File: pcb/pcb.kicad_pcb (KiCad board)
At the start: 2 copper layers, 60 x 30 mm, 30 parts, among them J1 USB_B_Mini, J2 Conn_01x04_Male, SW1 OS102011MA1QN1‎, SW1 PTS645Vx83, SW2 PTS645Vx83, SW3 PTS645Vx83, U1 AP2112K-3.3, U2 MIC5225-1.8YM5, U3 CP2104, U5 ESP-12F

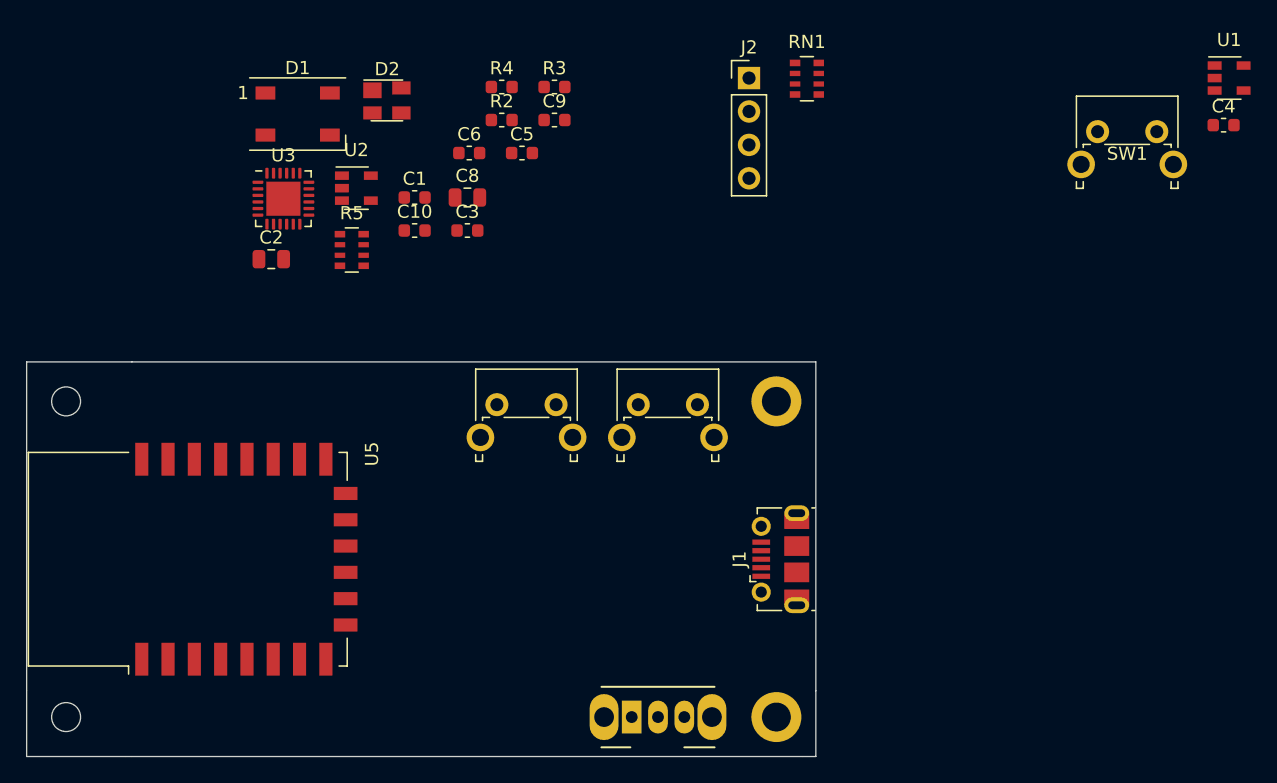
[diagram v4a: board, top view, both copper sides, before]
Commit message: finish laying out most of the pcb parts
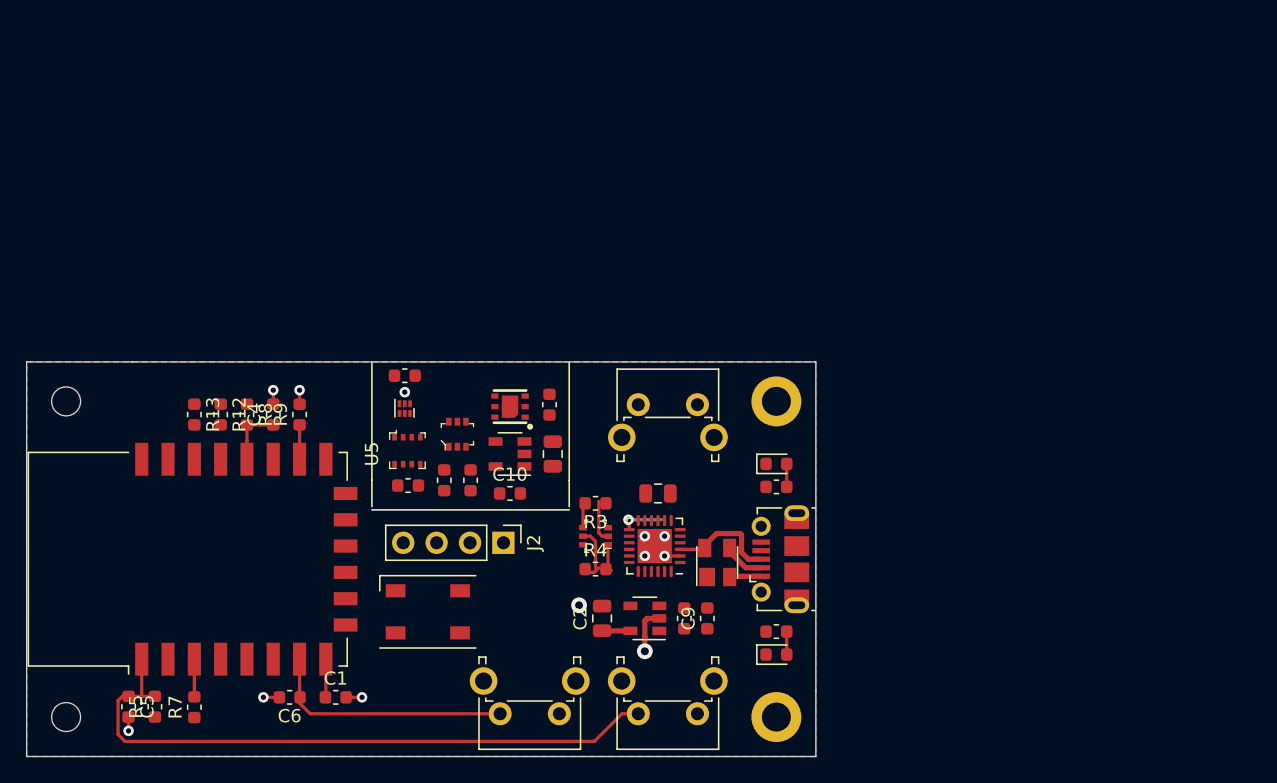
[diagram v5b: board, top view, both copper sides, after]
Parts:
- removed RN1: 10k, Resistor_SMD:R_Array_Convex_4x0603
- removed the SW1 at (86.0, 82.0)
- added C11: 100n, Capacitor_SMD:C_0603_1608Metric, F.Cu at (68.8, 56.0)
- added C12: 100n, Capacitor_SMD:C_0603_1608Metric, F.Cu at (79.8, 58.2)
- added C7: 10u, Capacitor_SMD:C_0805_2012Metric, F.Cu at (88.0, 65.0)
- added D3: LED, LED_SMD:LED_0603_1608Metric, F.Cu at (97.0, 62.8)
- added D4: LED, LED_SMD:LED_0603_1608Metric, F.Cu at (97.0, 77.2)
- added Q1: BSS138DW-7-F, digikey-footprints:SOT-363, F.Cu at (83.2, 68.2)
- added Q2: BSS138DW-7-F, digikey-footprints:SOT-363, F.Cu at (72.8, 60.5)
- added R1: 470, Resistor_SMD:R_0603_1608Metric, F.Cu at (97.0, 64.5)
- added R10: 10k, Resistor_SMD:R_0603_1608Metric, F.Cu at (71.8, 64.0)
- added R11: 10k, Resistor_SMD:R_0603_1608Metric, F.Cu at (73.8, 64.0)
- added R12: 10k, Resistor_SMD:R_0603_1608Metric, F.Cu at (54.8, 59.0)
- added R13: 10k, Resistor_SMD:R_0603_1608Metric, F.Cu at (52.8, 59.0)
- added R6: 470, Resistor_SMD:R_0603_1608Metric, F.Cu at (97.0, 75.5)
- added R7: 10k, Resistor_SMD:R_0603_1608Metric, F.Cu at (52.8, 81.2)
- added R8: 10k, Resistor_SMD:R_0603_1608Metric, F.Cu at (56.8, 59.0)
- added R9: 10k, Resistor_SMD:R_0603_1608Metric, F.Cu at (60.8, 59.0)
- added U4: BME280, digikey-footprints:Pressure_Sensor_LGA-8_2.5x2.5mm_BME280, F.Cu at (69.0, 61.8)
- added U6: SGP30, SGP30 (1):SGP30, F.Cu at (76.8, 58.4)
- added U7: TSL2591, Package_DFN_QFN:DFN-6_1.3x1.2mm_P0.4mm, F.Cu at (68.8, 58.5)
- C10: value 1u -> 10u
- C9: value 100n -> 10u
- R5: footprint Resistor_SMD:R_Array_Convex_4x0603 -> Resistor_SMD:R_0603_1608Metric
- moved C4 75.5 mm to (58.8, 59.0), turned to 90 degrees
- moved U1 60.5 mm to (87.0, 74.5), turned to 180 degrees
- moved SW1 60.3 mm to (80.5, 81.8), turned to 180 degrees
- moved C5 51.6 mm to (47.8, 81.2), turned to 270 degrees
- moved C6 43.6 mm to (60.0, 80.5), turned to 180 degrees
- moved D2 43.2 mm to (92.5, 70.2), turned to 90 degrees
- moved R2 40.4 mm to (90.0, 74.5), turned to 90 degrees
- moved J2 40.0 mm to (76.2, 68.8), turned to 270 degrees
- moved C9 39.6 mm to (91.8, 74.5), turned to 90 degrees
- moved D1 39.1 mm to (70.5, 74.0), turned to 180 degrees
- moved U3 38.7 mm to (87.8, 69.0), turned to 180 degrees
- moved C1 38.5 mm to (63.5, 80.5)
- moved R5 37.8 mm to (49.8, 81.2), turned to 90 degrees
- moved R4 37.3 mm to (83.2, 70.8)
- moved C2 37.1 mm to (83.8, 74.5), turned to 90 degrees
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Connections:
- C1 pad 1: nRST -> +3V3
- C3 pad 1: +5V -> +3V3
- C9 pad 1: +3V3 -> +5V
- D2 pad 2: Net-(D2-Pad2) -> +5V
- D2 pad 4: +5V -> Net-(D2-Pad4)
- J1 pad 3: Net-(D2-Pad2) -> Net-(D2-Pad4)
- R3 pad 1: (no net) -> Net-(Q1-Pad2)
- R4 pad 1: (no net) -> Net-(Q1-Pad5)
- R5 pad 1: Net-(R5-Pad1) -> +3V3
- SW1 pad 2: nBOOT -> MODE
- SW2 pad 2: nRST -> nBOOT
- SW3 pad 2: MODE -> nRST
- U2 pad 1: +3V3 -> +5V
- U2 pad 3: +3V3 -> +5V
- U3 pad 13: (no net) -> Net-(R1-Pad2)
- U3 pad 14: (no net) -> Net-(R6-Pad2)
- U3 pad 3: Net-(D2-Pad2) -> Net-(D2-Pad4)
- U5 pad 13: (no net) -> nINT
- U5 pad 14: MODE -> (no net)
- U5 pad 16: Net-(R5-Pad5) -> Net-(R9-Pad1)
- U5 pad 3: Net-(R5-Pad1) -> Net-(R7-Pad2)
- U5 pad 7: (no net) -> MODE
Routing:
- net nRST: track 0.00 -> 49.0 mm
- net MODE: track 0.00 -> 18.9 mm
- net GND: track 0.00 -> 14.0 mm, vias 0 -> 11
- net Net-(D2-Pad4): track 0.00 -> 8.37 mm
- net +3V3: track 0.00 -> 5.27 mm
- net nBOOT: track 0.00 -> 4.61 mm
- net Net-(Q1-Pad5): track 0.00 -> 4.05 mm
- net Net-(Q1-Pad2): track 0.00 -> 3.78 mm
- net Net-(R1-Pad2): track 0.00 -> 3.27 mm, vias 0 -> 1
- net Net-(D2-Pad3): track 0.00 -> 3.18 mm
- net Net-(R7-Pad2): track 0.00 -> 2.86 mm
- net Net-(R9-Pad1): track 0.00 -> 2.61 mm
- net Net-(Q1-Pad1): track 0.00 -> 2.26 mm
- net +5V: track 0.00 -> 2.17 mm
- net Net-(Q1-Pad4): track 0.00 -> 2.17 mm
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- added copper zone on F.Cu, net +3V3
- added copper zone on B.Cu, net GND

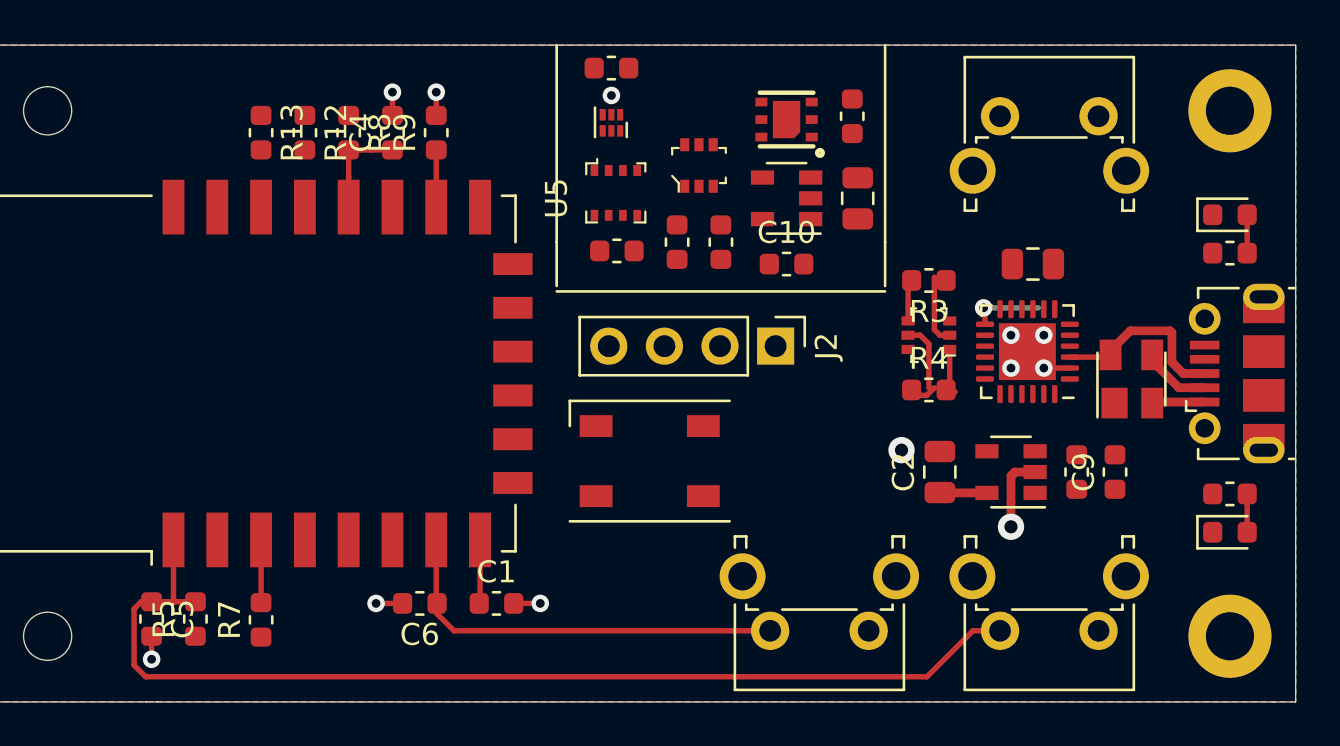
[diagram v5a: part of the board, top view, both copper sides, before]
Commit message: finish the routing of the pcb all that is left is to clean up the silkscreen
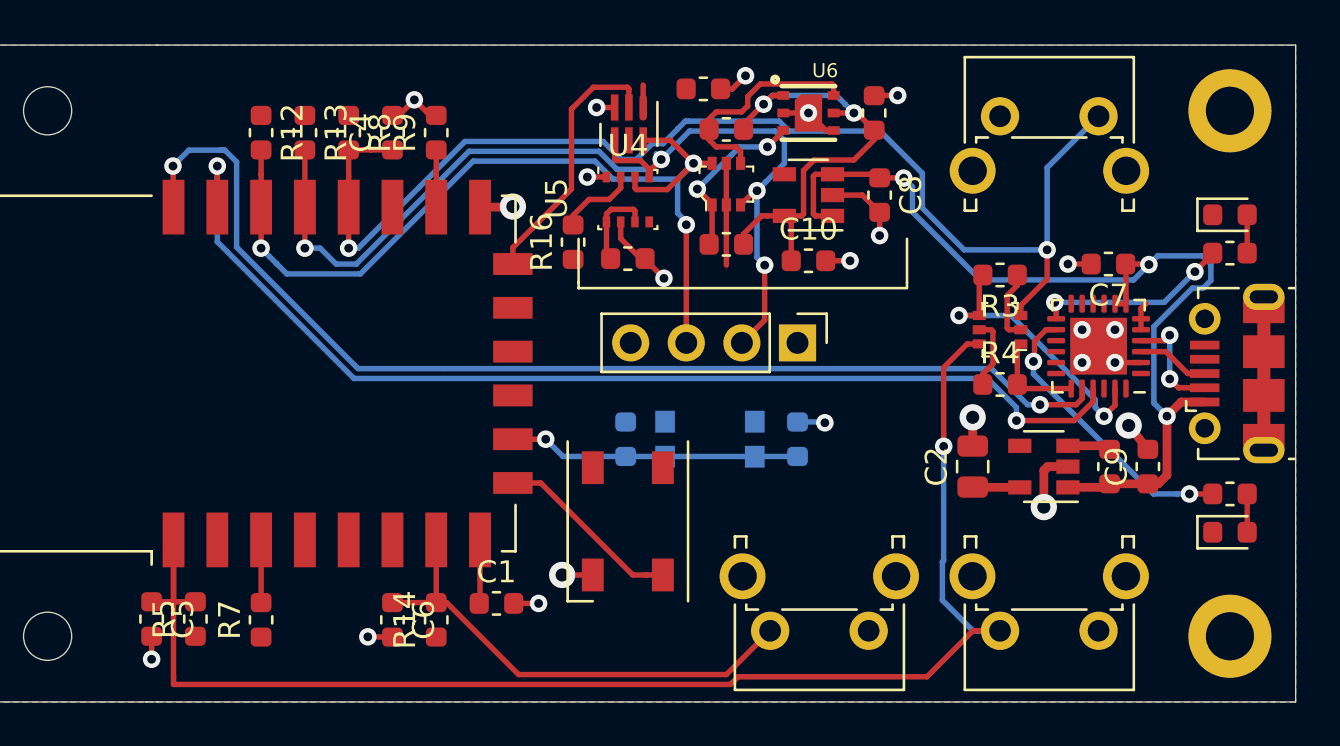
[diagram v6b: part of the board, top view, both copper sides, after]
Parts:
- removed D2: SP0503BAHT, Package_TO_SOT_SMD:SOT-143
- added C13: 100n, Capacitor_SMD:C_0603_1608Metric, B.Cu at (69.4, 73.0)
- added R14: 10k, Resistor_SMD:R_0603_1608Metric, F.Cu at (60.8, 81.2)
- added R15: 10k, Resistor_SMD:R_0603_1608Metric, B.Cu at (77.2, 73.0)
- added R16: 10k, Resistor_SMD:R_0603_1608Metric, F.Cu at (67.0, 64.0)
- added SW4: KMR2, Button_Switch_SMD:SW_Push_1P1T_NO_CK_KMR2, B.Cu at (73.2, 73.0)
- C7, C8: footprint Capacitor_SMD:C_0805_2012Metric -> Capacitor_SMD:C_0603_1608Metric
- U4: footprint digikey-footprints:Pressure_Sensor_LGA-8_2.5x2.5mm_BME280 -> Package_LGA:Bosch_LGA-8_2.5x2.5mm_P0.65mm_ClockwisePinNumbering
- U7: footprint Package_DFN_QFN:DFN-6_1.3x1.2mm_P0.4mm -> Kevin-Lutzer-Kicad-Lbr:TSL2591
- moved R11 5.16 mm to (74.0, 58.9), turned to 180 degrees
- moved C11 4.31 mm to (73.0, 57.0), turned to 0 degrees
- moved C7 3.45 mm to (91.5, 65.0)
- moved Q1 3.26 mm to (86.5, 68.0)
- moved R3 3.26 mm to (86.5, 65.5)
- moved R4 3.26 mm to (86.5, 70.5)
- moved U3 3.26 mm to (91.0, 68.8)
- moved D1 2.93 mm to (69.5, 76.8), turned to 270 degrees
- moved R10 2.25 mm to (74.0, 64.1), turned to 180 degrees
- moved R12 2.00 mm to (52.8, 59.0)
- moved R13 2.00 mm to (54.8, 59.0)
- moved C2 1.52 mm to (85.2, 74.2)
- moved C9 1.52 mm to (93.2, 74.2)
- moved R2 1.52 mm to (91.5, 74.2)
- moved U1 1.52 mm to (88.5, 74.2)
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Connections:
- net MODE renamed nMODE
- U4 pad 2: (no net) -> Net-(R16-Pad2)
- U5 pad 10: (no net) -> nFAC_RST
- U5 pad 13: nINT -> (no net)
- U5 pad 14: (no net) -> nINT
- U5 pad 17: RGB_LED -> (no net)
- U5 pad 9: (no net) -> RGB_LED
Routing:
- net UART_RX: track 0.00 -> 51.7 mm, vias 0 -> 2
- net nBOOT: track 4.61 -> 55.4 mm, vias 0 -> 2
- net UART_TX: track 0.00 -> 50.0 mm, vias 0 -> 2
- net I2C_SCK: track 0.00 -> 45.8 mm, vias 0 -> 4
- net I2C_SDA: track 0.00 -> 43.4 mm, vias 0 -> 3
- net +5V: track 2.17 -> 45.5 mm, vias 0 -> 3
- net GND: track 14.0 -> 39.7 mm, vias 11 -> 22
- net +1V8: track 0.00 -> 21.7 mm, vias 0 -> 2
- net nRST: track 49.0 -> 66.1 mm, vias 0 -> 1
- net nFAC_RST: track 0.00 -> 13.3 mm, vias 0 -> 1
- net Net-(R6-Pad2): track 0.07 -> 13.2 mm, vias 0 -> 2
- net +3V3: track 5.27 -> 17.5 mm, vias 0 -> 1
- net nINT: track 0.00 -> 12.1 mm, vias 1 -> 0
- net Net-(Q1-Pad4): track 2.17 -> 13.1 mm, vias 0 -> 2
- net I2C_SCK_1V8: track 0.00 -> 10.2 mm
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
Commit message: add gerbers for room monitor v1
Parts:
- added J4: UART_BUS, Connector_PinHeader_2.54mm:PinHeader_1x02_P2.54mm_Vertical, F.Cu at (47.5, 57.5)
- added REF**: OSHW-Symbol_6.7x6mm_SilkScreen, Symbol:OSHW-Symbol_6.7x6mm_SilkScreen, B.Cu at (57.8, 68.0)
- added REF**: KiCad-Logo_5mm_SilkScreen, Symbol:KiCad-Logo_5mm_SilkScreen, B.Cu at (54.8, 76.0)
- J2: value Conn_01x04_Male -> I2C_BUS
- moved R15 9.78 mm to (67.5, 73.8), turned to 90 degrees
- moved C13 6.15 mm to (75.5, 73.8), turned to 270 degrees
- moved SW4 1.90 mm to (71.5, 73.8), turned to 0 degrees
- moved C1 0.25 mm to (63.5, 80.2)
- moved C6 0.25 mm to (58.8, 81.0)
- moved R14 0.25 mm to (60.8, 81.0)
- moved R7 0.25 mm to (52.8, 81.0)
- moved C5 0.21 mm to (47.8, 81.0)
- moved R5 0.21 mm to (49.8, 81.0)
- turned D3 to 180 degrees
- turned D4 to 180 degrees
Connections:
- D3 pad 1: +3V3 -> Net-(D3-Pad1)
- D3 pad 2: Net-(D3-Pad2) -> +3V3
- D4 pad 1: +3V3 -> Net-(D4-Pad1)
- D4 pad 2: Net-(D4-Pad2) -> +3V3
- R1 pad 1: Net-(D3-Pad2) -> Net-(D3-Pad1)
- R6 pad 1: Net-(D4-Pad2) -> Net-(D4-Pad1)
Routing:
- net +1V8: track 21.7 -> 29.1 mm
- net GND: track 39.7 -> 47.0 mm
- net UART_RX: track 51.7 -> 55.2 mm
- net UART_TX: track 50.0 -> 53.3 mm
- net nMODE: track 22.3 -> 25.5 mm
- net nRST: track 66.1 -> 63.2 mm
- net nFAC_RST: track 13.3 -> 11.3 mm
- net Net-(D4-Pad2): track 2.00 -> 0.00 mm
- net Net-(D4-Pad1): track 0.00 -> 2.00 mm
- net Net-(D3-Pad2): track 2.00 -> 0.00 mm
- net Net-(D3-Pad1): track 0.00 -> 2.00 mm
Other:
- outline, holes or cut-outs redrawn
- board text added: "3.3V"
- board text added: "BOOT"
- board text added: "Designed With"
- board text added: "FAC_RST"
- board text added: "GND"
- board text added: "MODE"
- board text added: "RST"
- board text added: "RX"
- board text added: "Room Environment Monitor Kevin Luzer Rev A"
- board text added: "SCK"
- board text added: "SDA"
- board text added: "TX"

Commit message: make last minute changes
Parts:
- moved C4 0.40 mm to (58.8, 58.6)
- moved R12 0.40 mm to (52.8, 58.6)
- moved R13 0.40 mm to (54.8, 58.6)
- moved R8 0.40 mm to (56.8, 58.6)
- moved R9 0.40 mm to (60.8, 58.6)
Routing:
- net nBOOT: track 55.4 -> 52.0 mm
- net I2C_SDA: track 43.4 -> 40.2 mm
- net I2C_SCK: track 45.8 -> 43.9 mm
